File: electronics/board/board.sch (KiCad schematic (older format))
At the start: 2 parts

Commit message: Added some components and studied some datasheets.
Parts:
- added U? (x3): JW5211, Package_TO_SOT_SMD:SOT-23-5, symbol 3340_kicad:JW5211
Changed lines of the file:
@@
+	1    0    0    -1
+$EndComp
+$Comp
+L 3340_kicad:JW5211 U?
+U 1 1 60DF53BF
+P 10200 4050
+F 0 "U?" H 10200 4365 50  0000 C CNN
+F 1 "JW5211" H 10200 4274 50  0000 C CNN
+F 2 "Package_TO_SOT_SMD:SOT-23-5" H 10200 4350 50  0001 C CNN
+F 3 "https://datasheet.lcsc.com/szlcsc/1903011605_JoulWatt-Tech-JW5211_C371423.pdf" H 10200 4450 50  0001 C CNN
+	1    10200 4050
+	1    0    0    -1
+$EndComp
+$Comp
+L 3340_kicad:JW5211 U?
+U 1 1 60DF5C3E
+P 10200 4950
+F 0 "U?" H 10200 5265 50  0000 C CNN
+F 1 "JW5211" H 10200 5174 50  0000 C CNN
+F 2 "Package_TO_SOT_SMD:SOT-23-5" H 10200 5250 50  0001 C CNN
+F 3 "https://datasheet.lcsc.com/szlcsc/1903011605_JoulWatt-Tech-JW5211_C371423.pdf" H 10200 5350 50  0001 C CNN
+	1    10200 4950
+	1    0    0    -1
+$EndComp
+$Comp
+L 3340_kicad:JW5211 U?
+U 1 1 60DF6286
+P 10200 5800
+F 0 "U?" H 10200 6115 50  0000 C CNN
+F 1 "JW5211" H 10200 6024 50  0000 C CNN
+F 2 "Package_TO_SOT_SMD:SOT-23-5" H 10200 6100 50  0001 C CNN
+F 3 "https://datasheet.lcsc.com/szlcsc/1903011605_JoulWatt-Tech-JW5211_C371423.pdf" H 10200 6200 50  0001 C CNN
+	1    10200 5800
 	1    0    0    -1
 $EndComp

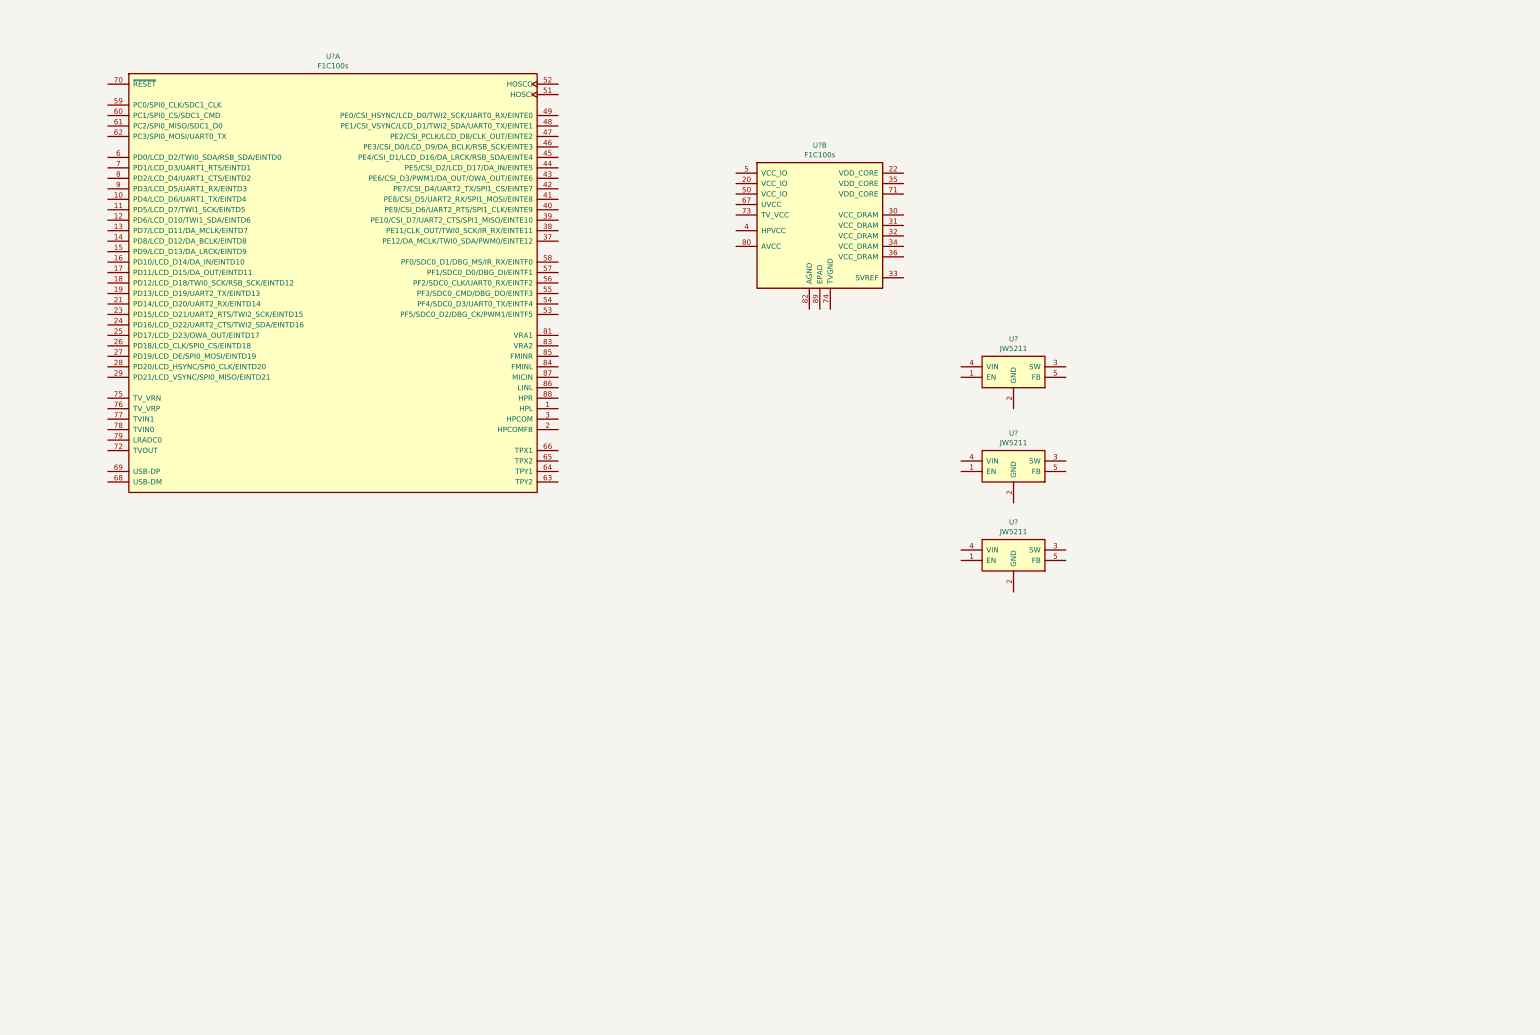
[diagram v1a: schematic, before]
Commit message: Dropped in the power supplies and hooked up the AP.
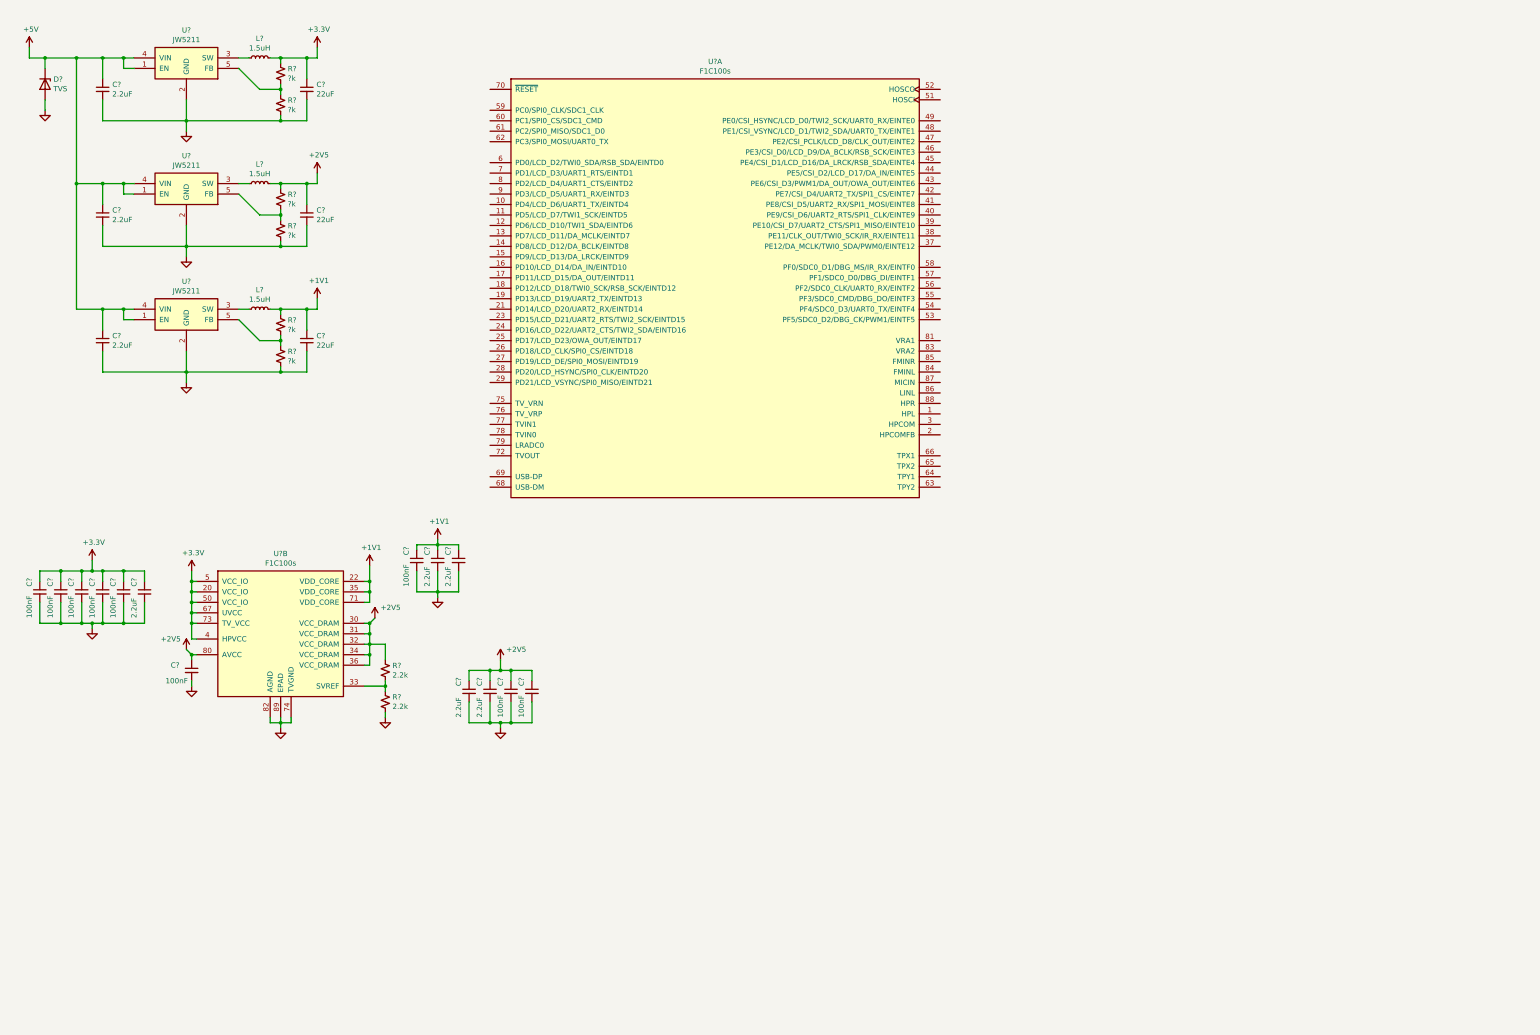
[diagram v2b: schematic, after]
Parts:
- removed U? (x2): JW5211, Package_TO_SOT_SMD:SOT-23-5, symbol 3340_kicad:JW5211
- added C? (x8): 2.2uF, symbol Device:C_Small
- added C? (x3): 22uF, symbol Device:C_Small
- added C? (x9): 100nF, symbol Device:C_Small
- added D?: TVS, symbol Device:D_Zener
- added L? (x3): 1.5uH, symbol Device:L_Small
- added R? (x6): ?k, symbol Device:R_Small_US
- added R? (x2): 2.2k, symbol Device:R_Small_US
- added U? (x2): JW5211, Package_TO_SOT_SMD:SOT-23-5, symbol 3340_kicad:JW5211
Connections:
- net +3V3: now reaches U?.20 (VCC_IO)
- net +3V3: now also U?.4 (HPVCC), U?.5 (VCC_IO), U?.50 (VCC_IO), U?.67 (UVCC), U?.73 (TV_VCC), C?.1, C?.1, C?.1, C?.1, C?.1, C?.1, C?.1, L?.2, R?.1
- net +1V1: now reaches U?.22 (VDD_CORE)
- net +1V1: now also U?.35 (VDD_CORE), U?.71 (VDD_CORE), C?.1, C?.1, C?.1, C?.1, L?.2, R?.1
- net +2V5: now reaches U?.30 (VCC_DRAM)
- net +2V5: now also U?.31 (VCC_DRAM), U?.32 (VCC_DRAM), U?.34 (VCC_DRAM), U?.36 (VCC_DRAM), U?.80 (AVCC), C?.1, C?.1, C?.1, C?.1, C?.1, C?.1, L?.2, R?.1, R?.1
- net at U?.33 (SVREF): now also R?.1, R?.2
- net GND: now reaches U?.74 (TVGND)
- net GND: now also U?.2 (GND), U?.82 (AGND), U?.89 (EPAD), C?.2, C?.2, C?.2, C?.2, C?.2, C?.2, C?.2, C?.2, C?.2, C?.2, C?.2, C?.2, C?.2, C?.2, C?.2, C?.2, C?.2, C?.2, C?.2, C?.2, D?.2 (A), R?.2, R?.2, R?.2, R?.2, U?.2 (GND), U?.2 (GND)
- net +5V: now reaches U?.1 (EN)
- net +5V: now also U?.4 (VIN), C?.1, C?.1, C?.1, D?.1 (K), U?.1 (EN), U?.1 (EN), U?.4 (VIN), U?.4 (VIN)
- net at U?.3 (SW): now also L?.1
- net at U?.5 (FB): now also R?.1, R?.2
- new net: L?.1, U?.3 (SW) (x2)
- new net: R?.1, R?.2, U?.5 (FB) (x2)
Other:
- moved on the sheet: U?, U?A, U?B

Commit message: Flash in, header in, UART in, Crystal in. Wired up most of the board.
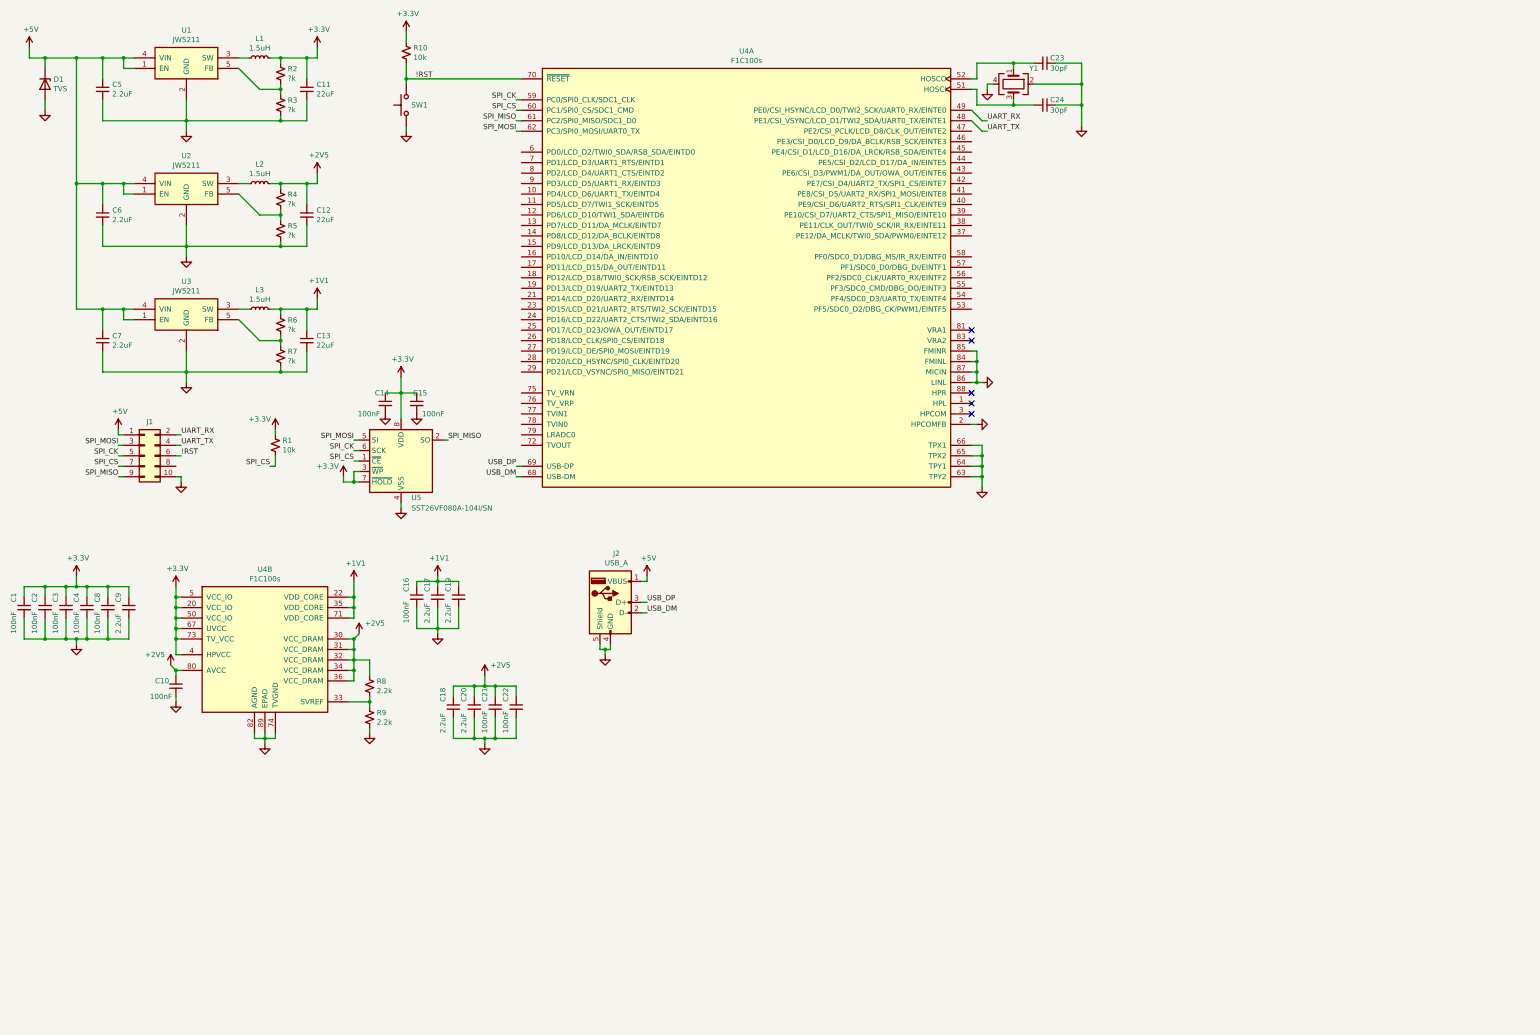
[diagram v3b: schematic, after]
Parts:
- added C14, C15: 100nF, symbol Device:C_Small
- added C23, C24: 30pF, symbol Device:C_Small
- added J1: Conn_02x05_Odd_Even, symbol Connector_Generic:Conn_02x05_Odd_Even
- added J2: USB_A, symbol Connector:USB_A
- added R1, R10: 10k, symbol Device:R_Small_US
- added SW1: SW_Push, symbol Switch:SW_Push
- added U5: SST26VF080A-104I/SN, Package_SO:SOIC-8_5.275x5.275mm_P1.27mm, symbol Memory_Flash:SST25VF080B-50-4x-S2Ax
- added Y1: Crystal_GND24, symbol Device:Crystal_GND24
- gave numbers to parts that had none: 36
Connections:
- net +3V3: now also C14.1, C15.1, R1.1, R10.1, U5.3 (~WP~), U5.7 (~HOLD~), U5.8 (VDD)
- net +5V: now also J1.1 (Pin_1), J2.1 (VBUS)
- net GND: now also U4.2 (HPCOMFB), U4.63 (TPY2), U4.64 (TPY1), U4.65 (TPX2), U4.66 (TPX1), U4.84 (FMINL), U4.85 (FMINR), U4.86 (LINL), U4.87 (MICIN), C14.2, C15.2, C23.1, C24.1, J1.10 (Pin_10), J2.4 (GND), J2.5 (Shield), SW1.1, U5.4 (VSS), Y1.2, Y1.4
- net UART_TX: now reaches U4.48 (PE1/CSI_VSYNC/LCD_D1/TWI2_SDA/UART0_TX/EINTE1)
- net UART_TX: now also J1.4 (Pin_4)
- net UART_RX: now reaches U4.49 (PE0/CSI_HSYNC/LCD_D0/TWI2_SCK/UART0_RX/EINTE0)
- net UART_RX: now also J1.2 (Pin_2)
- net at U4.51 (HOSCI): now also C24.2, Y1.3
- net at U4.52 (HOSCO): now also C23.2, Y1.1
- net SPI_CK: now reaches U4.59 (PC0/SPI0_CLK/SDC1_CLK)
- net SPI_CK: now also J1.5 (Pin_5), U5.6 (SCK)
- net SPI_CS: now reaches U4.60 (PC1/SPI0_CS/SDC1_CMD)
- net SPI_CS: now also J1.7 (Pin_7), R1.2, U5.1 (~CE)
- net SPI_MISO: now reaches U4.61 (PC2/SPI0_MISO/SDC1_D0)
- net SPI_MISO: now also J1.9 (Pin_9), U5.2 (SO)
- net SPI_MOSI: now reaches U4.62 (PC3/SPI0_MOSI/UART0_TX)
- net SPI_MOSI: now also J1.3 (Pin_3), U5.5 (SI)
- net USB_DM: now reaches U4.68 (USB-DM)
- net USB_DM: now also J2.2 (D-)
- net USB_DP: now reaches U4.69 (USB-DP)
- net USB_DP: now also J2.3 (D+)
- net !RST: now reaches U4.70 (~RESET)
- net !RST: now also J1.6 (Pin_6), R10.2, SW1.2
- no-connect marks 0 -> 5
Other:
- moved on the sheet: C1, C10, C16, C17, C18, C19, C2, C20, C21, C22, C3, C4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

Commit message: Added user manual, dropped in SD card holder into schematic.
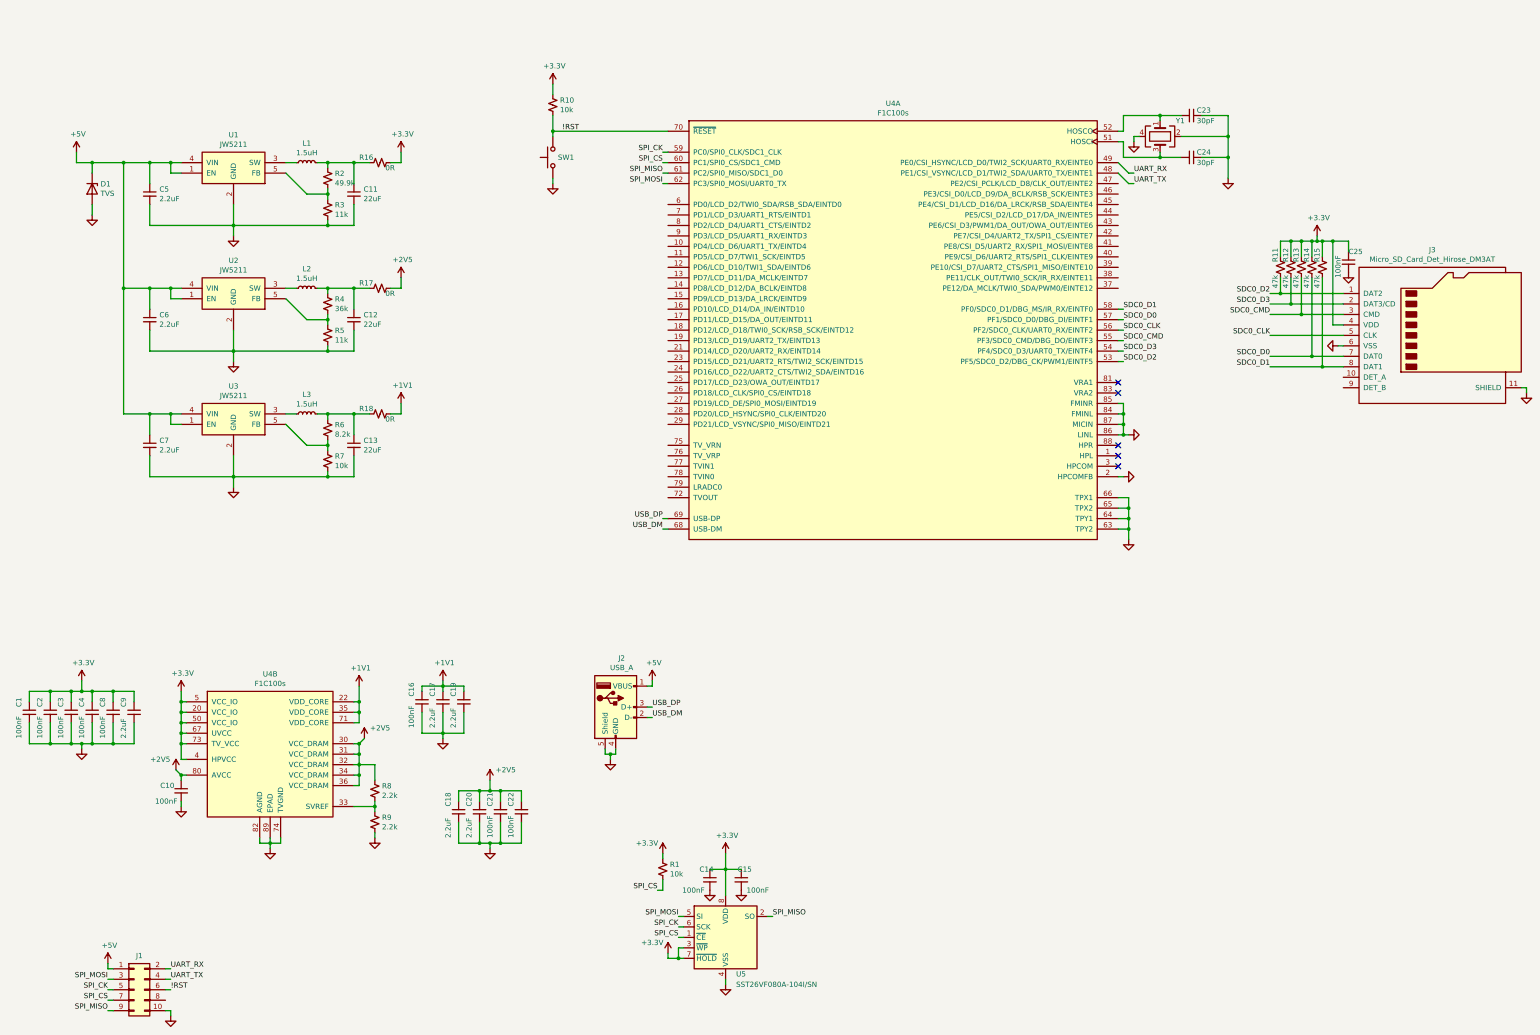
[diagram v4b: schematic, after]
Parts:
- added C25: 100nF, symbol Device:C_Small
- added J3: Micro_SD_Card_Det_Hirose_DM3AT, Connector_Card:microSD_HC_Hirose_DM3AT-SF-PEJM5, symbol Connector:Micro_SD_Card_Det_Hirose_DM3AT
- added R11, R12, R13, R14, R15: 47k, symbol Device:R_Small_US
- added R16, R17, R18: 0R, symbol Device:R_Small_US
- R2: value ?k -> 49.9k
- R3, R5: value ?k -> 11k
- R4: value ?k -> 36k
- R6: value ?k -> 8.2k
- R7: value ?k -> 10k
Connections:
- net +1V1: now also R18.1; no longer C13.1, L3.2, R6.1
- net +2V5: now also R17.1; no longer C12.1, L2.2, R4.1
- net +3V3: now also C25.1, J3.4 (VDD), R11.1, R12.1, R13.1, R14.1, R15.1, R16.1; no longer C11.1, L1.2, R2.1
- net GND: now also C25.2, J3.11 (SHIELD), J3.6 (VSS)
- net SDC0_D2: now reaches U4.53 (PF5/SDC0_D2/DBG_CK/PWM1/EINTF5)
- net SDC0_D2: now also J3.1 (DAT2), R11.2
- net SDC0_D3: now reaches U4.54 (PF4/SDC0_D3/UART0_TX/EINTF4)
- net SDC0_D3: now also J3.2 (DAT3/CD), R12.2
- net SDC0_CMD: now reaches U4.55 (PF3/SDC0_CMD/DBG_DO/EINTF3)
- net SDC0_CMD: now also J3.3 (CMD), R13.2
- net SDC0_CLK: now reaches U4.56 (PF2/SDC0_CLK/UART0_RX/EINTF2)
- net SDC0_CLK: now also J3.5 (CLK)
- net SDC0_D0: now reaches U4.57 (PF1/SDC0_D0/DBG_DI/EINTF1)
- net SDC0_D0: now also J3.7 (DAT0), R14.2
- net SDC0_D1: now reaches U4.58 (PF0/SDC0_D1/DBG_MS/IR_RX/EINTF0)
- net SDC0_D1: now also J3.8 (DAT1), R15.2
- new net: C11.1, L1.2, R16.2, R2.1
- new net: C12.1, L2.2, R17.2, R4.1
- new net: C13.1, L3.2, R18.2, R6.1
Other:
- moved on the sheet: C1, C10, C11, C12, C13, C14, C15, C16, C17, C18, C19, C2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
